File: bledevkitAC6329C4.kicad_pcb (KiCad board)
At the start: 2 copper layers, 41.1 x 39.1 mm, 32 parts, among them J1 USB_C_Receptacle_USB2.0_16P, J2 Conn_01x02, J4 Conn_01x07, J5 Qwiic_I2C_connector, J6 Conn_01x07, J7 Conn_01x02, J8 Conn_01x01, SW1 SW_DPDT_x2, SW2 SW_DPDT_x2, SW3 SW_Push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

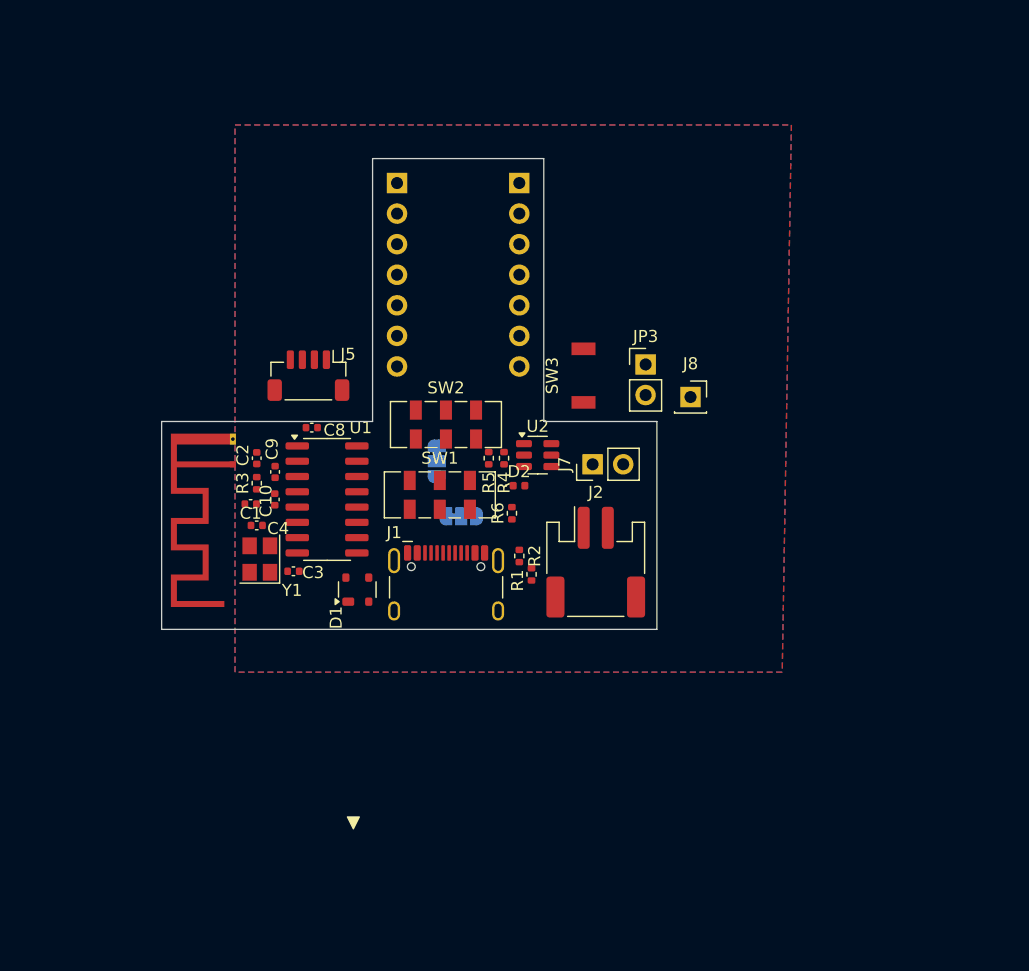
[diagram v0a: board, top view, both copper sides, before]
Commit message: Finalized power topology
Isolated all power draws other than AC6329 behind current probe point.  Added auxiliary 3.3V regulator as an option for Qwiic header.  Shouldn't need any schematic changes, just on to making things fit and adding the switch footprints.
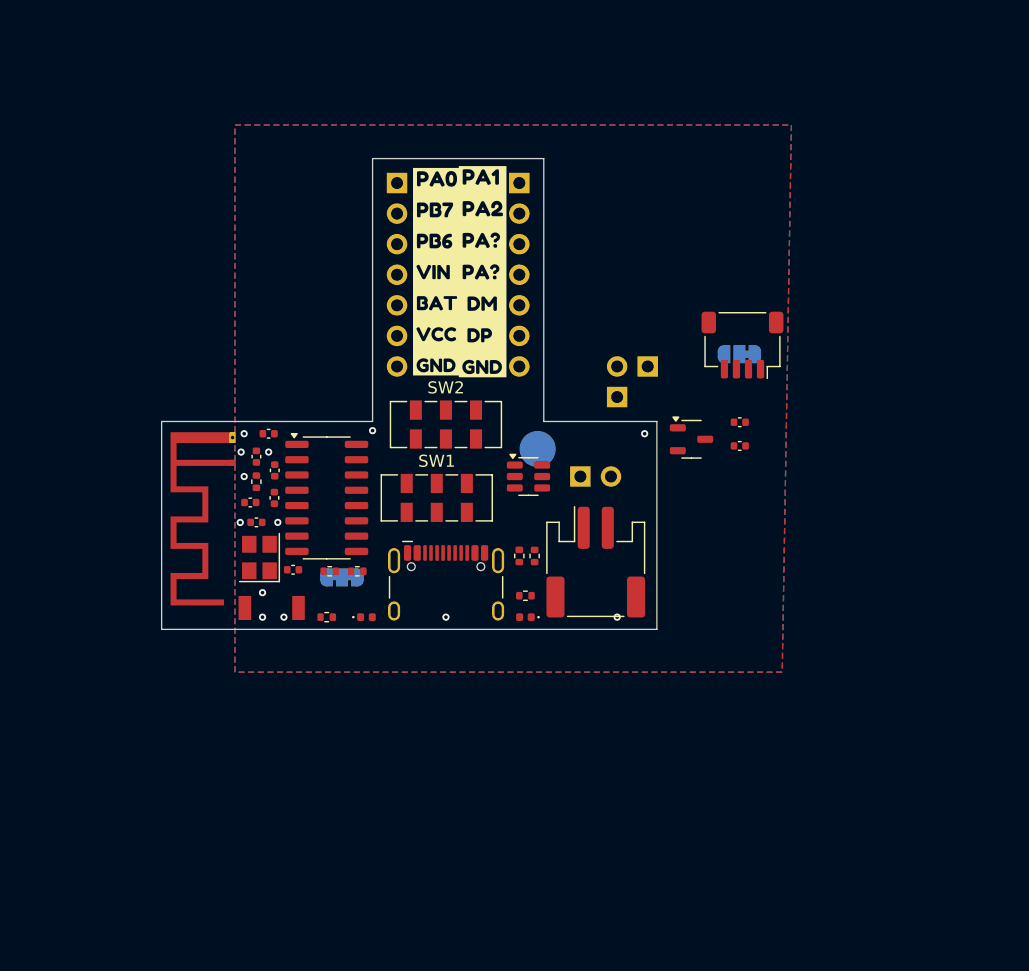
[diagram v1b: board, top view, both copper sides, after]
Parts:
- removed D1: ESDUSB, Package_TO_SOT_SMD:SOT-143
- added C5: 1u, Capacitor_SMD:C_0402_1005Metric, F.Cu at (109.0, 45.5)
- added C6: 1u, Capacitor_SMD:C_0402_1005Metric, F.Cu at (109.0, 47.5)
- added D3: LED, LED_SMD:LED_0402_1005Metric, F.Cu at (91.2, 61.7)
- added R7: 510, Resistor_SMD:R_0402_1005Metric, F.Cu at (91.2, 59.9)
- added TP1: TestPoint, TestPoint:TestPoint_Pad_D3.0mm, B.Cu at (92.2, 47.8)
- added U3: XC6206, Package_TO_SOT_SMD:SOT-23-3, F.Cu at (105.0, 46.9)
- added kibuzzard-667E2D83: G***, kibuzzard-667E2D83, F.Cu at (83.8, 33.0)
- added kibuzzard-667E2DB2: G***, kibuzzard-667E2DB2, F.Cu at (87.6, 33.0)
- J5: footprint Connector_JST:JST_SH_BM04B-SRSS-TB_1x04-1MP_P1.00mm_Vertical -> Connector_JST:JST_SH_SM04B-SRSS-TB_1x04-1MP_P1.00mm_Horizontal
- J8: footprint Connector_PinSocket_2.54mm:PinSocket_1x01_P2.54mm_Vertical -> Connector_PinHeader_2.54mm:PinHeader_1x01_P2.54mm_Vertical
- moved J5 36.2 mm to (109.2, 39.1)
- moved SW3 32.3 mm to (70.1, 61.0), turned to 180 degrees
- moved JP1 26.7 mm to (109.0, 39.9), turned to 180 degrees
- moved R6 17.6 mm to (74.7, 61.7), turned to 0 degrees
- moved D2 16.7 mm to (78.0, 61.7)
- moved R5 16.2 mm to (74.9, 57.9), turned to 180 degrees
- moved R4 15.4 mm to (77.2, 57.9), turned to 0 degrees
- moved JP2 11.1 mm to (75.9, 58.4), turned to 0 degrees
- moved J8 4.37 mm to (101.3, 40.9)
- moved C8 3.62 mm to (69.8, 46.5)
- moved JP3 3.59 mm to (98.8, 43.4), turned to 180 degrees
- moved U2 1.93 mm to (91.4, 50.0)
- moved R1 1.55 mm to (91.9, 56.6)
- moved J7 1.44 mm to (95.8, 50.0)
- moved SW1 0.36 mm to (83.8, 51.8)
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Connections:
- C8 pad 1: /PB5 -> VIN
- C9 pad 1: Net-(SW2B-B) -> +BATT
- J1 pad A4: /VIN -> VBUS
- J1 pad A9: /VIN -> VBUS
- J1 pad B4: /VIN -> VBUS
- J1 pad B9: /VIN -> VBUS
- J2 pad 1: +BATT -> Net-(J2-Pin_1)
- J4 pad 4: /PB5 -> VIN
- J7 pad 1: +BATT -> Net-(J2-Pin_1)
- JP1 pad 3: +BATT -> AUX
- JP3 pad 1: /VIN -> VSW
- JP3 pad 2: VBUS -> VIN
- SW2 pad 2: /PB5 -> VSW
- SW2 pad 4: +BATT -> Net-(J2-Pin_1)
- SW2 pad 5: Net-(SW2B-B) -> +BATT
- U1 pad 2: /PB5 -> VIN
- U1 pad 3: Net-(SW2B-B) -> +BATT
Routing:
- net GND: vias 0 -> 13
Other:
- board text removed: "Qwiic Power"
- board text removed: "VCC"
- board text removed: "VSW"

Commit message: Finalized switches, chose modern DFU trigger
Switched to the newest series of the ATTINY line for UPDI programming, which can be done over the USB-C connector for simplicity of flashing.  Also made custom footprints for SMD DPDT slide switches.  Temp routing 80% done.
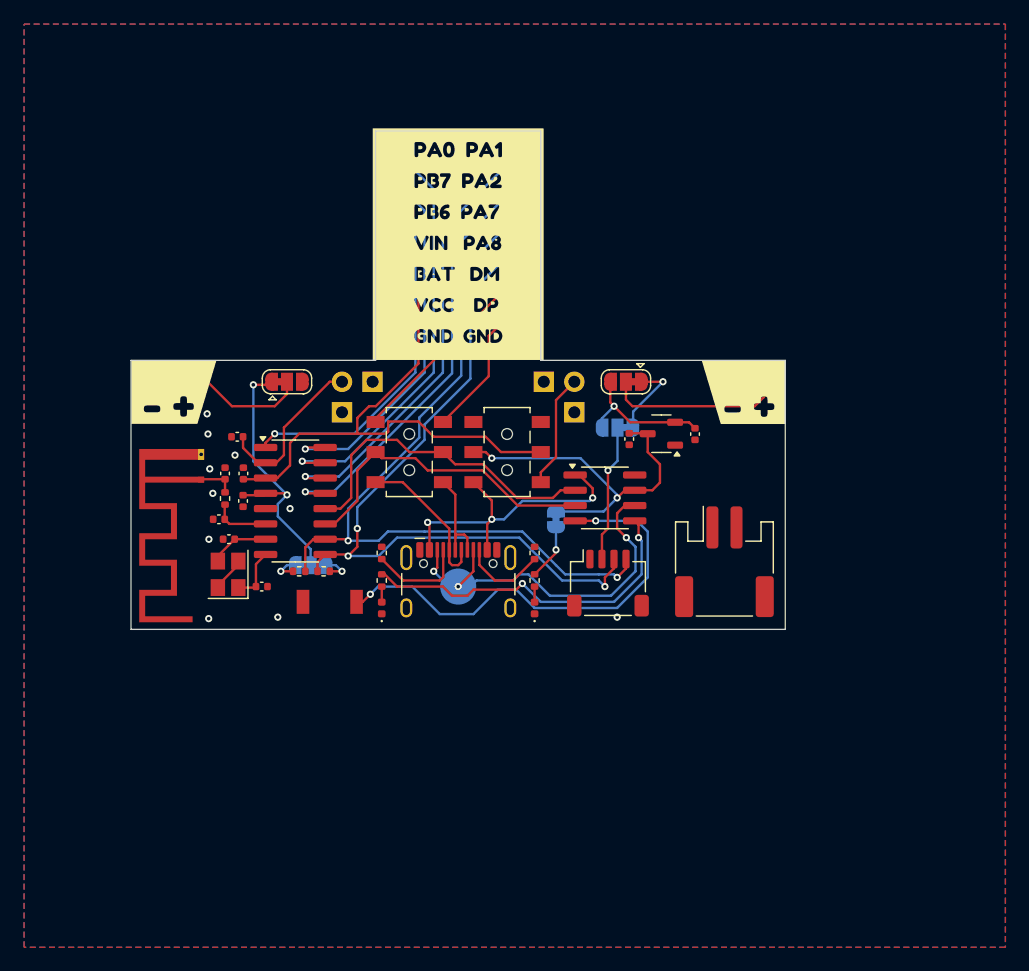
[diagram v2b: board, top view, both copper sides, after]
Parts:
- removed U2: ATtiny10-TS, Package_TO_SOT_SMD:SOT-23-6
- removed kibuzzard-667E2D83: G***, kibuzzard-667E2D83
- removed kibuzzard-667E2DB2: G***, kibuzzard-667E2DB2
- added J3: Conn_01x02, Connector_PinHeader_2.54mm:PinHeader_1x02_P2.54mm_Vertical, B.Cu at (62.7, 42.2)
- added J9: Conn_01x02, Connector_PinHeader_2.54mm:PinHeader_1x02_P2.54mm_Vertical, B.Cu at (111.0, 42.2)
- added JP4: SolderJumper_3_Bridged12, Jumper:SolderJumper-3_P1.3mm_Bridged12_RoundedPad1.0x1.5mm, F.Cu at (71.4, 42.2)
- added JP5: SolderJumper_3_Bridged12, Jumper:SolderJumper-3_P1.3mm_Bridged12_RoundedPad1.0x1.5mm, F.Cu at (99.5, 42.2)
- added JP6: Jumper_2_Bridged, Connector_PinHeader_2.54mm:PinHeader_1x02_P2.54mm_Vertical, F.Cu at (95.2, 44.7)
- added JP7: SolderJumper_2_Bridged, Jumper:SolderJumper-2_P1.3mm_Bridged_RoundedPad1.0x1.5mm, B.Cu at (93.7, 53.6)
- added U4: ATtiny202-SS, Package_SO:SOIC-8_3.9x4.9mm_P1.27mm, F.Cu at (97.8, 51.8)
- added kibuzzard-667FBBEE: G***, kibuzzard-667FBBEE, F.Cu at (109.3, 43.0)
- added kibuzzard-667FBC34: G***, kibuzzard-667FBC34, F.Cu at (62.0, 43.0)
- added kibuzzard-667FBD1F: G***, kibuzzard-667FBD1F, F.Cu at (85.6, 30.7)
- J7: value Conn_01x02 -> Conn_01x01; footprint Connector_PinHeader_2.54mm:PinHeader_1x02_P2.54mm_Vertical -> Connector_PinHeader_2.54mm:PinHeader_1x01_P2.54mm_Vertical
- SW1, SW2: footprint Button_Switch_SMD:SW_DPDT_CK_JS202011JCQN -> maxfootprints:DPDT-Slide_top
- moved J8 22.9 mm to (78.5, 42.2)
- moved JP3 22.9 mm to (75.9, 44.7)
- moved J5 22.7 mm to (98.0, 58.9), turned to 0 degrees
- moved TP1 13.2 mm to (85.6, 59.2)
- moved R1 12.7 mm to (79.2, 56.4)
- moved JP1 11.8 mm to (98.8, 46.0)
- moved J2 10.7 mm to (107.7, 57.1)
- moved C5 9.29 mm to (99.8, 46.9), turned to -90 degrees
- moved J7 8.44 mm to (92.7, 42.2), turned to 0 degrees
- moved SW2 5.57 mm to (89.7, 48.0), turned to 90 degrees
- moved R6 5.50 mm to (79.2, 58.7), turned to 90 degrees
- moved SW3 4.85 mm to (74.9, 60.5)
- moved SW1 4.44 mm to (81.5, 48.0), turned to 90 degrees
- moved C6 3.85 mm to (105.3, 46.5), turned to -90 degrees
- moved C2 2.96 mm to (66.2, 49.8)
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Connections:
- D2 pad 1: Net-(D2-K) -> GND
- D2 pad 2: VBUS -> Net-(D2-A)
- D3 pad 1: Net-(D3-K) -> GND
- D3 pad 2: VSW -> Net-(D3-A)
- J1 pad A8: +BATT -> /UPDI
- J1 pad B8: /CASE -> /UPDI
- J7 pad 1: Net-(J2-Pin_1) -> GND
- R6 pad 1: /BUT -> Net-(D2-A)
- R6 pad 2: Net-(D2-K) -> /LED
- R7 pad 1: GND -> Net-(D3-A)
- R7 pad 2: Net-(D3-K) -> Net-(JP7-B)
- SW2 pad 4: Net-(J2-Pin_1) -> Net-(JP6-B)
- TP1 pad 1: /RST -> /UPDI
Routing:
- net /SCL: track 0.00 -> 65.0 mm, vias 0 -> 2
- net /SDA: track 0.00 -> 61.7 mm, vias 0 -> 3
- net +BATT: track 0.00 -> 45.7 mm
- net /BUT: track 0.00 -> 38.4 mm, vias 0 -> 2
- net /PA1: track 0.00 -> 37.6 mm, vias 0 -> 1
- net /PA2: track 0.00 -> 36.1 mm, vias 0 -> 1
- net /PA0: track 0.00 -> 35.5 mm, vias 0 -> 1
- net /UPDI: track 0.00 -> 31.9 mm, vias 0 -> 3
- net /PB7: track 0.00 -> 30.9 mm, vias 0 -> 1
- net VCC: track 0.00 -> 29.6 mm, vias 0 -> 3
- net VSW: track 0.00 -> 29.3 mm, vias 0 -> 2
- net /PB6: track 0.00 -> 29.1 mm, vias 0 -> 1
- net /LED: track 0.00 -> 29.0 mm, vias 0 -> 2
- net /DP: track 0.00 -> 27.5 mm
- net /DM: track 0.00 -> 26.6 mm
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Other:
- board size 41.1 x 39.1 mm -> 54.4 x 41.4 mm

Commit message: Finished routing
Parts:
- removed kibuzzard-667FBD1F: G***, kibuzzard-667FBD1F
- added G***: LOGO, LOGO, F.Cu at (109.5, 48.8)
- added kibuzzard-66809CDB: G***, kibuzzard-66809CDB, F.Cu at (89.4, 53.6)
- added kibuzzard-66809CF2: G***, kibuzzard-66809CF2, F.Cu at (88.9, 42.9)
- added kibuzzard-66809D04: G***, kibuzzard-66809D04, F.Cu at (81.8, 42.9)
- added kibuzzard-66809D18: G***, kibuzzard-66809D18, F.Cu at (81.8, 53.6)
- added kibuzzard-66809D78: G***, kibuzzard-66809D78, F.Cu at (93.3, 60.0)
- added kibuzzard-66809D9A: G***, kibuzzard-66809D9A, F.Cu at (107.7, 51.8)
- added kibuzzard-66809DBE: G***, kibuzzard-66809DBE, F.Cu at (102.6, 58.9)
- added kibuzzard-66809E23: G***, kibuzzard-66809E23, F.Cu at (71.4, 45.0)
- added kibuzzard-66809E23: G***, kibuzzard-66809E23, B.Cu at (98.8, 48.8)
- added kibuzzard-6680A820: G***, kibuzzard-6680A820, F.Cu at (78.0, 60.2)
- added kibuzzard-6680A94E: G***, kibuzzard-6680A94E, F.Cu at (99.6, 45.0)
- added kibuzzard-6680AAC4: G***, kibuzzard-6680AAC4, F.Cu at (67.6, 61.0)
- added kibuzzard-6680ABE0: G***, kibuzzard-6680ABE0, B.Cu at (85.9, 61.0)
- added kibuzzard-6680AC8C: G***, kibuzzard-6680AC8C, B.Cu at (102.6, 47.3)
- added kibuzzard-6680AE53: G***, kibuzzard-6680AE53, B.Cu at (81.8, 42.2)
- added kibuzzard-6680AE53: G***, kibuzzard-6680AE53, B.Cu at (89.9, 42.2)
- added kibuzzard-6680B177: G***, kibuzzard-6680B177, F.Cu at (85.6, 30.9)
- added kibuzzard-6680B7C1: G***, kibuzzard-6680B7C1, B.Cu at (72.9, 43.4)
- added kibuzzard-6680B7CF: G***, kibuzzard-6680B7CF, B.Cu at (98.0, 42.9)
- added kibuzzard-6680BA41: G***, kibuzzard-6680BA41, B.Cu at (98.0, 56.4)
- added kibuzzard-6680BA59: G***, kibuzzard-6680BA59, B.Cu at (73.3, 54.8)
- added kibuzzard-6680BEA0: G***, kibuzzard-6680BEA0, B.Cu at (108.5, 51.6)
- moved C5 4.74 mm to (103.4, 50.0), turned to 0 degrees
- moved JP7 3.31 mm to (95.5, 56.4)
- moved C6 1.53 mm to (106.4, 47.5)
- moved U3 1.53 mm to (103.6, 47.5)
- moved SW3 1.52 mm to (73.4, 60.5)
- moved TP1 1.02 mm to (85.6, 58.2)
- moved J2 0.59 mm to (108.0, 57.7)
- moved Y1 0.27 mm to (66.7, 58.0)
- moved C3 0.08 mm to (69.4, 59.2), turned to -90 degrees
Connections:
- J2 pad 1: Net-(J2-Pin_1) -> /EXT
- JP6 pad 1: Net-(J2-Pin_1) -> Net-(JP6-A)
- JP6 pad 2: Net-(JP6-B) -> +BATT
- SW2 pad 4: Net-(JP6-B) -> /EXT
- SW2 pad 5: +BATT -> Net-(JP6-A)
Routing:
- net VCC: track 29.6 -> 72.4 mm, vias 3 -> 5
- net AUX: track 11.8 -> 42.9 mm, vias 1 -> 2
- net VSW: track 29.3 -> 57.8 mm, vias 2 -> 3
- net VIN: track 13.8 -> 34.6 mm
- net /EXT: track 0.00 -> 18.3 mm, vias 0 -> 2
- net +BATT: track 45.7 -> 63.0 mm
- net Net-(JP6-B): track 9.50 -> 0.00 mm
- net Net-(JP6-A): track 0.00 -> 4.68 mm
- net /IODM: track 17.2 -> 21.8 mm
- net /PB7: track 30.9 -> 33.0 mm
- net /PB6: track 29.1 -> 31.2 mm
- net GND: track 2.90 -> 4.84 mm, vias 12 -> 37
- net /IODP: track 12.3 -> 13.9 mm
- net /PA0: track 35.5 -> 36.9 mm
- net /UPDI: track 31.9 -> 30.7 mm
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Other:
- board size 54.4 x 41.4 mm -> 54.4 x 40.9 mm

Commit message: Initial BOM and Finalized graphics
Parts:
- added G***: LOGO, LOGO, B.Cu at (68.1, 53.8)
- added kibuzzard-6680DFC0: G***, kibuzzard-6680DFC0, B.Cu at (109.8, 44.3)
- added kibuzzard-6680DFC0: G***, kibuzzard-6680DFC0, B.Cu at (61.6, 44.2)
- added kibuzzard-6680E09B: G***, kibuzzard-6680E09B, B.Cu at (85.6, 30.7)
- U4: value ATtiny202-SS -> ATtiny412-SSNR
- moved kibuzzard-6680BEA0 0.76 mm to (107.7, 51.6)

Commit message: Started DFM optimization
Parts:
- turned SW2 to -90 degrees
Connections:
- SW2 pad 1: VBUS -> unconnected-(SW2A-A-Pad1)
- SW2 pad 2: VSW -> Net-(JP6-A)
- SW2 pad 3: unconnected-(SW2A-C-Pad3) -> /EXT
- SW2 pad 4: /EXT -> unconnected-(SW2B-A-Pad4)
- SW2 pad 5: Net-(JP6-A) -> VSW
- SW2 pad 6: unconnected-(SW2B-C-Pad6) -> VBUS
